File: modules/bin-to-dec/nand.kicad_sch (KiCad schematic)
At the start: 6 parts, among them Q13 DMP3099L, Q14 2N7002, Q15 2N7002, Q16 2N7002, Q17 DMP3099L, Q18 DMP3099L

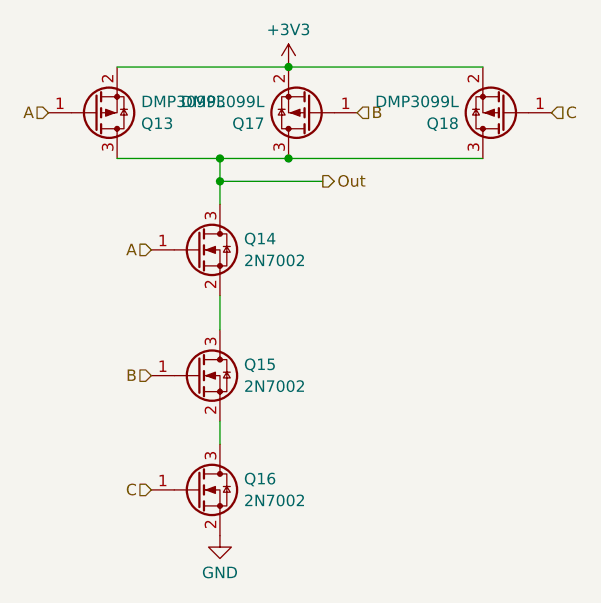
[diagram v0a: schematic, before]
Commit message: move to correct dir. improved symmetry of pcb
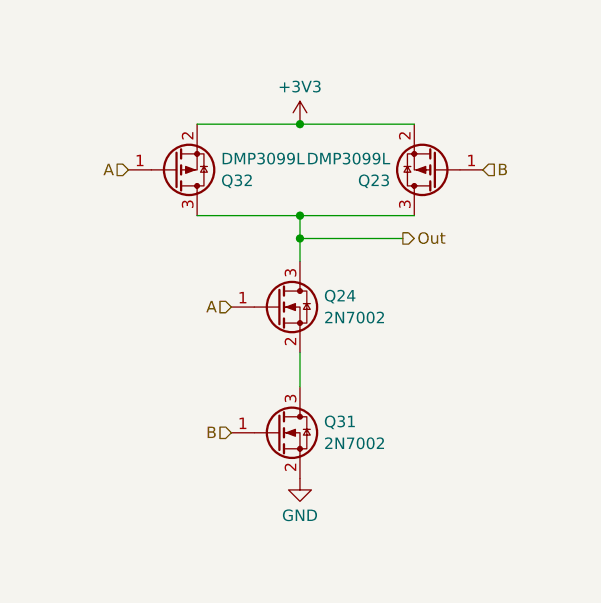
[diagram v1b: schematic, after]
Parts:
- removed Q13, Q17, Q18: DMP3099L, Package_TO_SOT_SMD:SOT-23, symbol Transistor_FET:DMP3099L
- removed Q14, Q15, Q16: 2N7002, Package_TO_SOT_SMD:SOT-23, symbol Transistor_FET:2N7002
- added Q23, Q32: DMP3099L, Package_TO_SOT_SMD:SOT-23, symbol Transistor_FET:DMP3099L
- added Q24, Q31: 2N7002, Package_TO_SOT_SMD:SOT-23, symbol Transistor_FET:2N7002
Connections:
- net +3V3: now also Q23.2 (S), Q32.2 (S)
- net A: now also Q24.1 (G), Q32.1 (G)
- net B: now also Q23.1 (G), Q31.1 (G)
- net GND: now also Q31.2 (S)
- net Out: now also Q23.3 (D), Q24.3 (D), Q32.3 (D)
- new net: Q24.2 (S), Q31.3 (D)

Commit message: using plugin to generate jlc production files
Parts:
- Q23, Q32: LCSC Part # (none) -> C2940610
- Q24, Q31: LCSC Part # (none) -> C8545
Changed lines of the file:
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@@
+			)
+		)
+		(property "LCSC Part #" "C8545"
+			(at 144.78 90.17 0)
+			(effects
+				(font
+					(size 1.27 1.27)
+				)
+				(hide yes)
 			)
 		)
@@
 		)
 		(property "Description" "-3.8A Id, -30V Vds, P-Channel MOSFET, SOT-23"
+			(at 162.56 60.96 0)
+			(effects
+				(font
+					(size 1.27 1.27)
+				)
+				(hide yes)
+			)
+		)
+		(property "LCSC Part #" "C2940610"
 			(at 162.56 60.96 0)
 			(effects
@@
 			)
 		)
+		(property "LCSC Part #" "C8545"
+			(at 144.78 76.2 0)
+			(effects
+				(font
+					(size 1.27 1.27)
+				)
+				(hide yes)
+			)
+		)
 		(pin "1"
 		)
@@
 			(at 133.35 60.96 0)
 			(effects
+				(font
+					(size 1.27 1.27)
+				)
+				(hide yes)
+			)
+		)
+		(property "LCSC Part #" "C2940610"
+			(at 133.35 60.96 0)
+			(effects

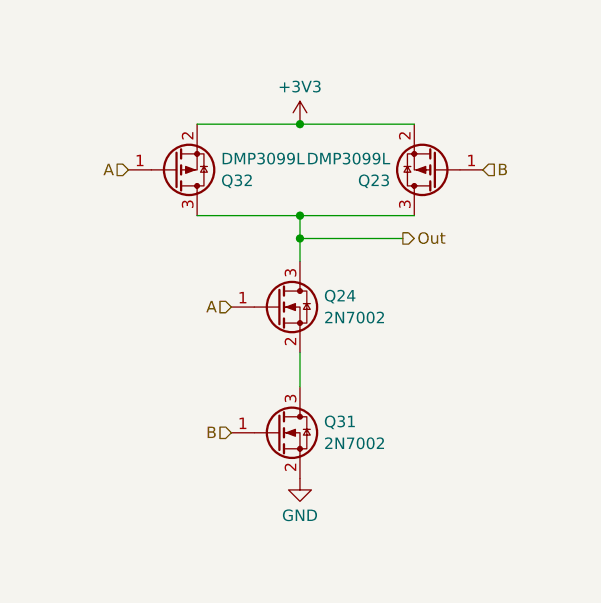
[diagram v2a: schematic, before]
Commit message: move components to top layer :(
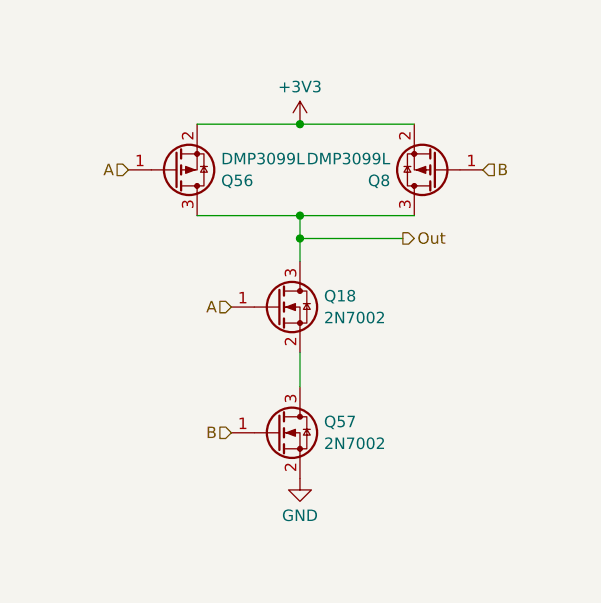
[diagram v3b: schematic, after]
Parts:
- Q18: renamed from Q24; LCSC part number (none) -> C8545
- Q56: renamed from Q32; LCSC part number (none) -> C2940610
- Q57: renamed from Q31; LCSC part number (none) -> C8545
- Q8: renamed from Q23; LCSC part number (none) -> C2940610
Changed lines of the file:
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@@
 		(dnp no)
 		(fields_autoplaced yes)
-		(property "Reference" "Q31"
+		(property "Reference" "Q57"
 			(at 149.987 88.9578 0)
 			(effects
@@
 		)
 		(property "LCSC Part #" "C8545"
+			(at 144.78 90.17 0)
+			(effects
+				(font
+					(size 1.27 1.27)
+				)
+				(hide yes)
+			)
+		)
+		(property "LCSC part number" "C8545"
 			(at 144.78 90.17 0)
 			(effects
@@
 			(project "bin-to-dec"
 				(path "/b244e12b-f85f-4579-ba5e-848643f54694/8559444b-ed80-4591-94fd-530ce32ce577"
+					(reference "Q46")
+					(unit 1)
+				)
+				(path "/b244e12b-f85f-4579-ba5e-848643f54694/9ee95dfd-f3ee-48c6-9665-30ae2b1f5b54"
+					(reference "Q19")
+					(unit 1)
+				)
+				(path "/b244e12b-f85f-4579-ba5e-848643f54694/c84f6135-6667-4c7e-9ce8-5338f93253d6"
 					(reference "Q57")
-					(unit 1)
-				)
-				(path "/b244e12b-f85f-4579-ba5e-848643f54694/9ee95dfd-f3ee-48c6-9665-30ae2b1f5b54"
-					(reference "Q67")
-					(unit 1)
-				)
-				(path "/b244e12b-f85f-4579-ba5e-848643f54694/c84f6135-6667-4c7e-9ce8-5338f93253d6"
-					(reference "Q31")
 					(unit 1)
 				)
@@
 		(on_board yes)
 		(dnp no)
-		(property "Reference" "Q23"
+		(property "Reference" "Q8"
 			(at 157.353 62.1722 0)
 			(effects
@@
 		)
 		(property "LCSC Part #" "C2940610"
+			(at 162.56 60.96 0)
+			(effects
+				(font
+					(size 1.27 1.27)
+				)
+				(hide yes)
+			)
+		)
+		(property "LCSC part number" "C2940610"
 			(at 162.56 60.96 0)
 			(effects
@@
 			(project "bin-to-dec"
 				(path "/b244e12b-f85f-4579-ba5e-848643f54694/8559444b-ed80-4591-94fd-530ce32ce577"
-					(reference "Q52")
+					(reference "Q50")
 					(unit 1)
 				)
 				(path "/b244e12b-f85f-4579-ba5e-848643f54694/9ee95dfd-f3ee-48c6-9665-30ae2b1f5b54"
-					(reference "Q65")
+					(reference "Q27")
 					(unit 1)
 				)
 				(path "/b244e12b-f85f-4579-ba5e-848643f54694/c84f6135-6667-4c7e-9ce8-5338f93253d6"
-					(reference "Q23")
+					(reference "Q8")
 					(unit 1)
 				)
@@
 		(dnp no)
 		(fields_autoplaced yes)
-		(property "Reference" "Q24"
+		(property "Reference" "Q18"
 			(at 149.987 74.9878 0)
 			(effects
@@
 		)
 		(property "LCSC Part #" "C8545"
+			(at 144.78 76.2 0)
+			(effects
+				(font
+					(size 1.27 1.27)
+				)
+				(hide yes)
+			)
+		)
+		(property "LCSC part number" "C8545"
 			(at 144.78 76.2 0)
 			(effects
@@
 			(project "bin-to-dec"
 				(path "/b244e12b-f85f-4579-ba5e-848643f54694/8559444b-ed80-4591-94fd-530ce32ce577"
-					(reference "Q53")
+					(reference "Q51")
 					(unit 1)
 				)
 				(path "/b244e12b-f85f-4579-ba5e-848643f54694/9ee95dfd-f3ee-48c6-9665-30ae2b1f5b54"
-					(reference "Q66")
+					(reference "Q25")
 					(unit 1)
 				)
 				(path "/b244e12b-f85f-4579-ba5e-848643f54694/c84f6135-6667-4c7e-9ce8-5338f93253d6"
-					(reference "Q24")
+					(reference "Q18")
 					(unit 1)
 				)
@@
 		(on_board yes)
 		(dnp no)
-		(property "Reference" "Q32"
+		(property "Reference" "Q56"
 			(at 138.557 62.1722 0)
 			(effects
@@
 		)
 		(property "LCSC Part #" "C2940610"
+			(at 133.35 60.96 0)
+			(effects
+				(font
+					(size 1.27 1.27)
+				)
+				(hide yes)
+			)
+		)
+		(property "LCSC part number" "C2940610"
 			(at 133.35 60.96 0)
 			(effects
@@
 			(project "bin-to-dec"
 				(path "/b244e12b-f85f-4579-ba5e-848643f54694/8559444b-ed80-4591-94fd-530ce32ce577"
-					(reference "Q58")
+					(reference "Q53")
 					(unit 1)
 				)
 				(path "/b244e12b-f85f-4579-ba5e-848643f54694/9ee95dfd-f3ee-48c6-9665-30ae2b1f5b54"
-					(reference "Q68")
+					(reference "Q26")
 					(unit 1)
 				)
 				(path "/b244e12b-f85f-4579-ba5e-848643f54694/c84f6135-6667-4c7e-9ce8-5338f93253d6"
-					(reference "Q32")
-					(unit 1)
-				)
+					(reference "Q56")
+					(unit 1)
+				)

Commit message: switched to jlc basic components
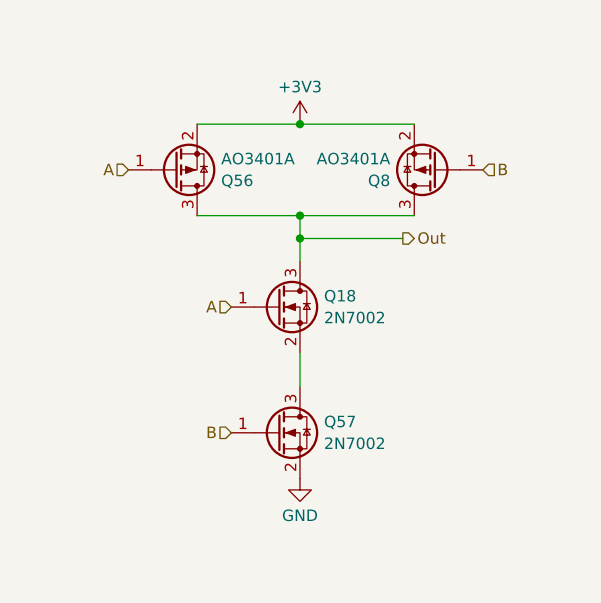
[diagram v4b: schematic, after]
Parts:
- Q56, Q8: value DMP3099L -> AO3401A; LCSC Part # C2940610 -> C15127
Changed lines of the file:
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@@
 			)
 		)
-		(property "Value" "DMP3099L"
+		(property "Value" "AO3401A"
 			(at 157.353 59.7479 0)
 			(effects
@@
 			)
 		)
-		(property "Datasheet" "https://www.diodes.com/assets/Datasheets/DMP3099L.pdf"
+		(property "Datasheet" "https://jlcpcb.com/api/file/downloadByFileSystemAccessId/8553305450243108864"
 			(at 157.48 57.15 0)
 			(effects
@@
 			)
 		)
-		(property "LCSC Part #" "C2940610"
+		(property "LCSC Part #" "C15127"
 			(at 162.56 60.96 0)
 			(effects
@@
 			)
 		)
-		(property "Value" "DMP3099L"
+		(property "Value" "AO3401A"
 			(at 138.557 59.7479 0)
 			(effects
@@
 			)
 		)
-		(property "Datasheet" "https://www.diodes.com/assets/Datasheets/DMP3099L.pdf"
+		(property "Datasheet" "https://jlcpcb.com/api/file/downloadByFileSystemAccessId/8553305450243108864"
 			(at 138.43 57.15 0)
 			(effects
@@
 			)
 		)
-		(property "LCSC Part #" "C2940610"
+		(property "LCSC Part #" "C15127"
 			(at 133.35 60.96 0)
 			(effects

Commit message: minor edits
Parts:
- Q18, Q57: LCSC part number C8545 -> (none)
- Q56, Q8: LCSC part number C2940610 -> (none)
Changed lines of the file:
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@@
-			)
-		)
-		(property "LCSC part number" "C8545"
-			(at 144.78 90.17 0)
-			(effects
-				(font
-					(size 1.27 1.27)
-				)
-				(hide yes)
 			)
 		)
@@
 		)
 		(property "LCSC Part #" "C15127"
-			(at 162.56 60.96 0)
-			(effects
-				(font
-					(size 1.27 1.27)
-				)
-				(hide yes)
-			)
-		)
-		(property "LCSC part number" "C2940610"
 			(at 162.56 60.96 0)
 			(effects
@@
 			)
 		)
-		(property "LCSC part number" "C8545"
-			(at 144.78 76.2 0)
-			(effects
-				(font
-					(size 1.27 1.27)
-				)
-				(hide yes)
-			)
-		)
 		(pin "1"
 		)
@@
 			(at 133.35 60.96 0)
 			(effects
-				(font
-					(size 1.27 1.27)
-				)
-				(hide yes)
-			)
-		)
-		(property "LCSC part number" "C2940610"
-			(at 133.35 60.96 0)
-			(effects
